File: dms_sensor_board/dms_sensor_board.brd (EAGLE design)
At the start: 44.5 x 44.5 mm, 24 parts, among them Q1 IRLML5203

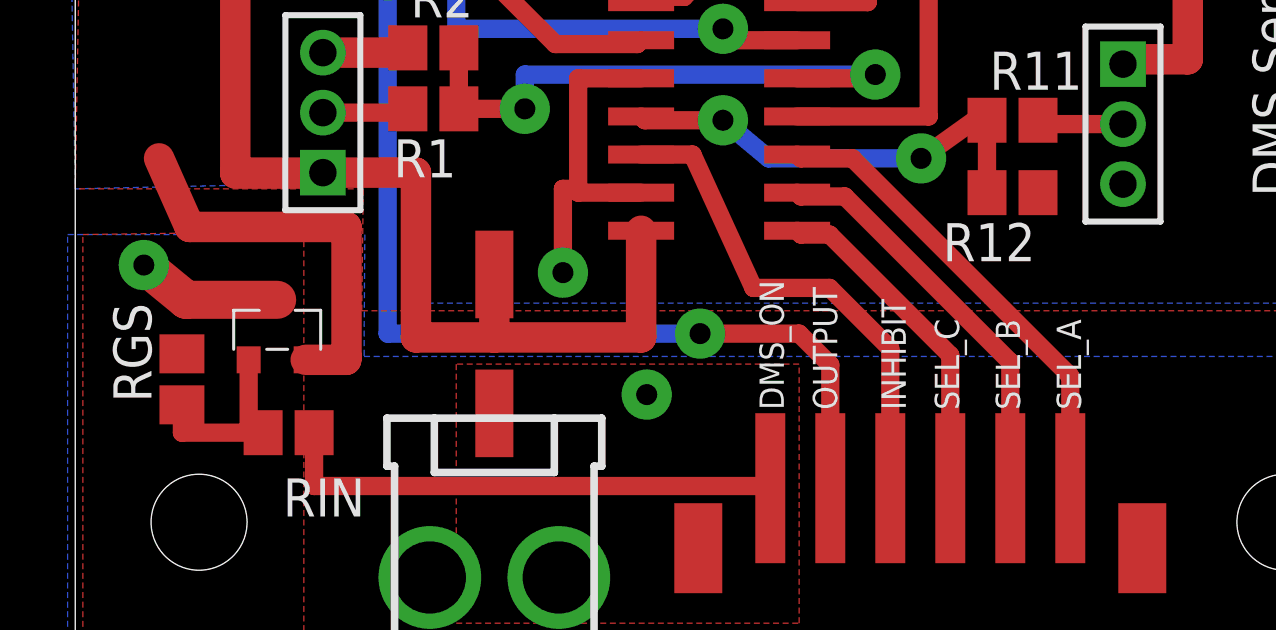
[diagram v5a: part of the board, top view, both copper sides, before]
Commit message: hole size, wire distance fixes, no soldermask changes yet
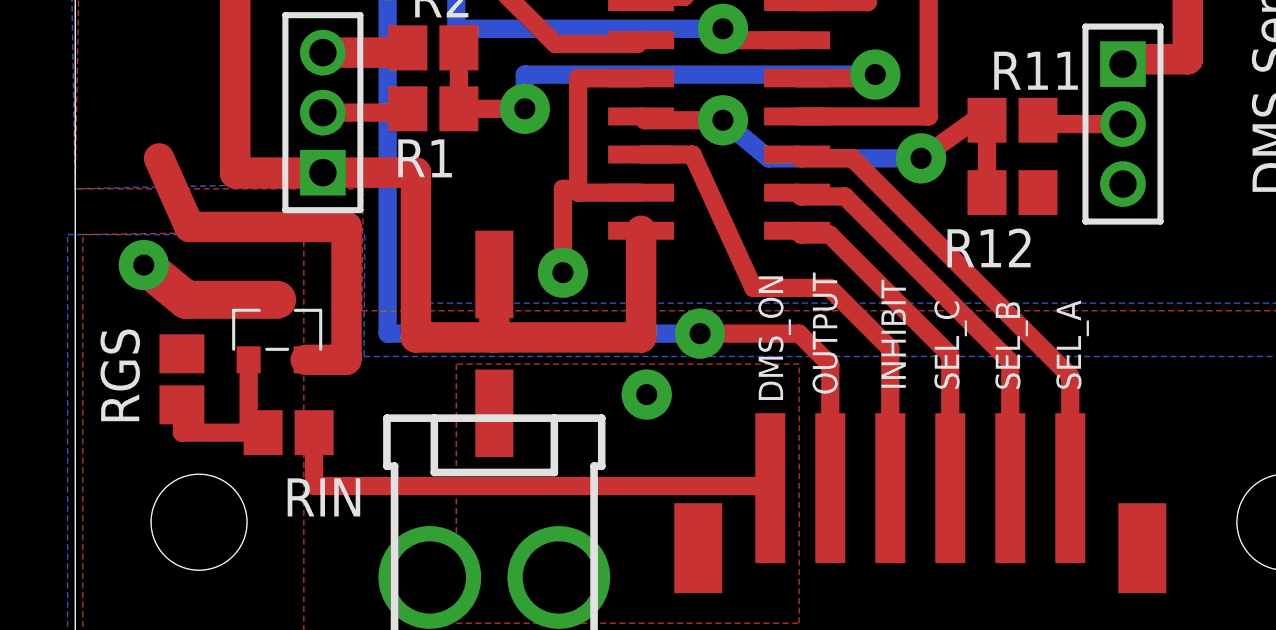
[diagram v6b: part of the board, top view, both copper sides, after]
